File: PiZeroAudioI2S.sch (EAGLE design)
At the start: 52 parts, among them CN1 1X4-BIG, CON1 RPI-ZERO, J1 1X2-3.5MM, Q1 DMG2305UX, U1 TXB0104PWR, U2 LSM6DS33, U3 PCM5101A, U4 TPA3144D2PWPR, U5 DMMT5401

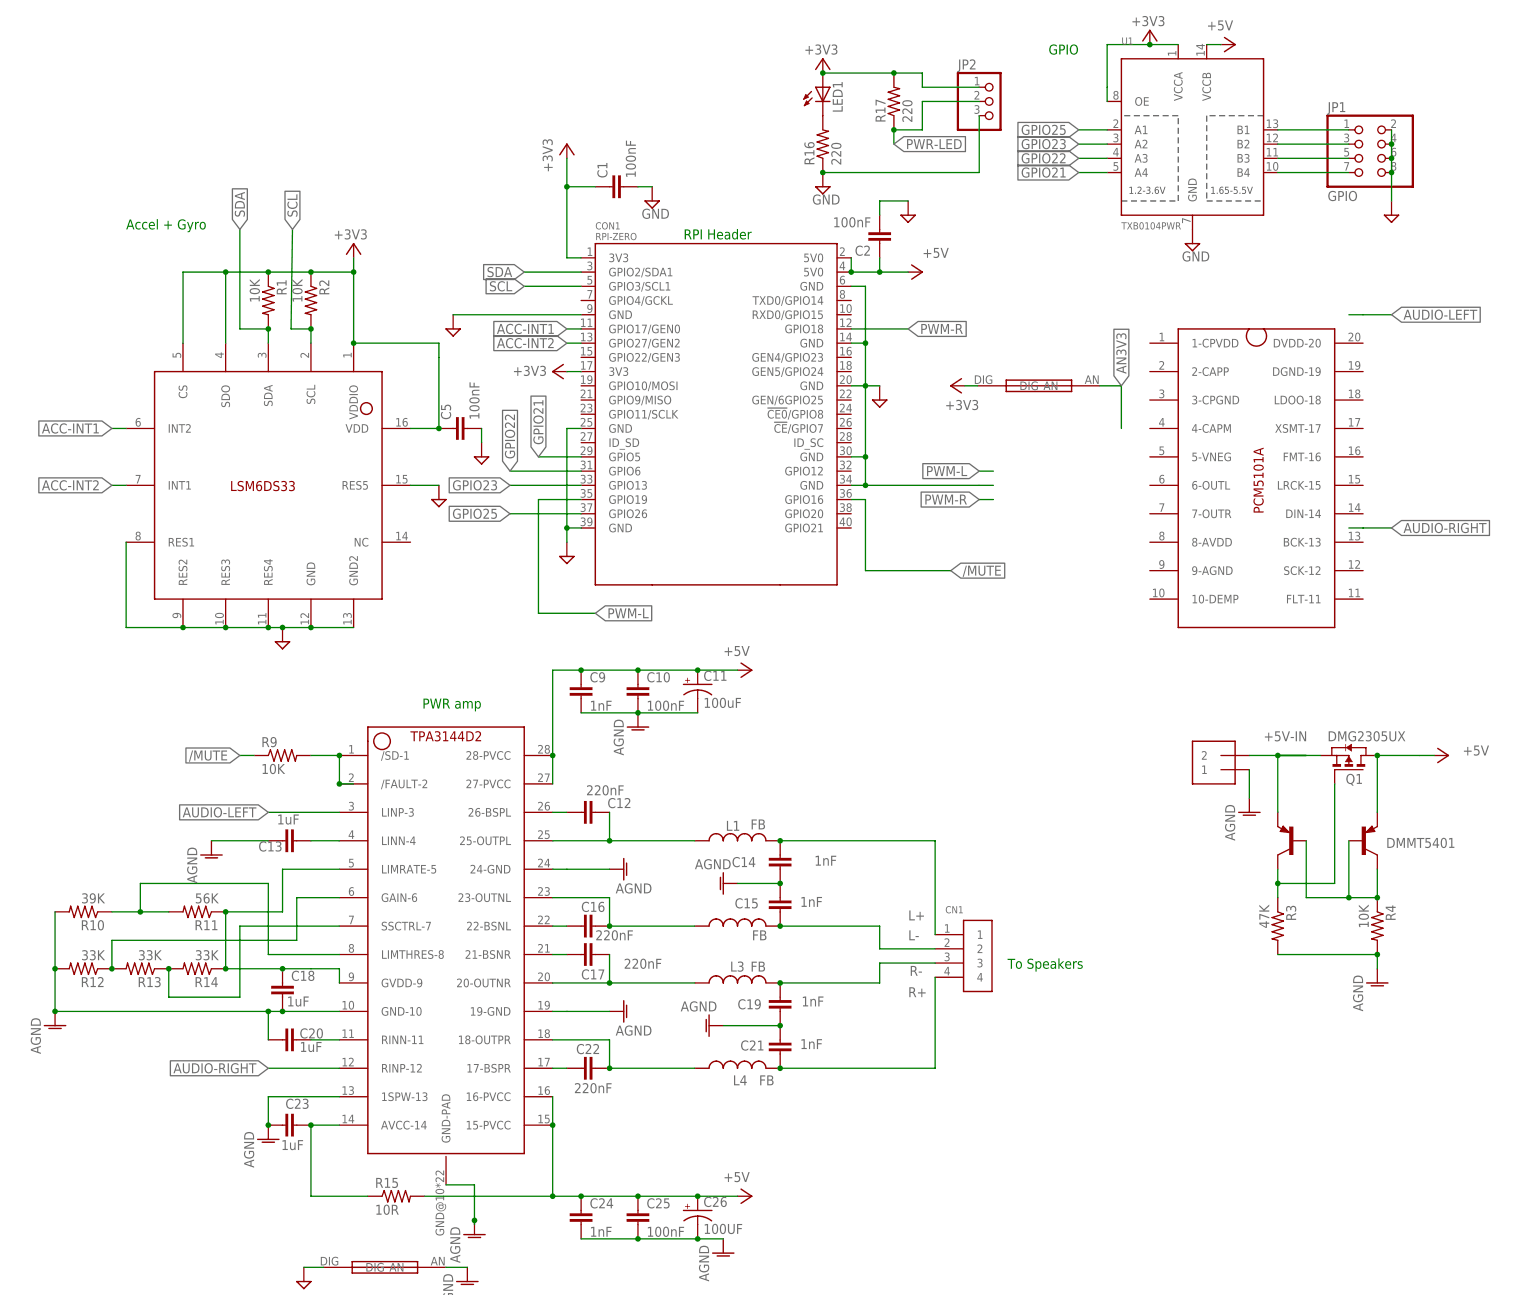
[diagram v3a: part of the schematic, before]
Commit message: Added I2Sboard
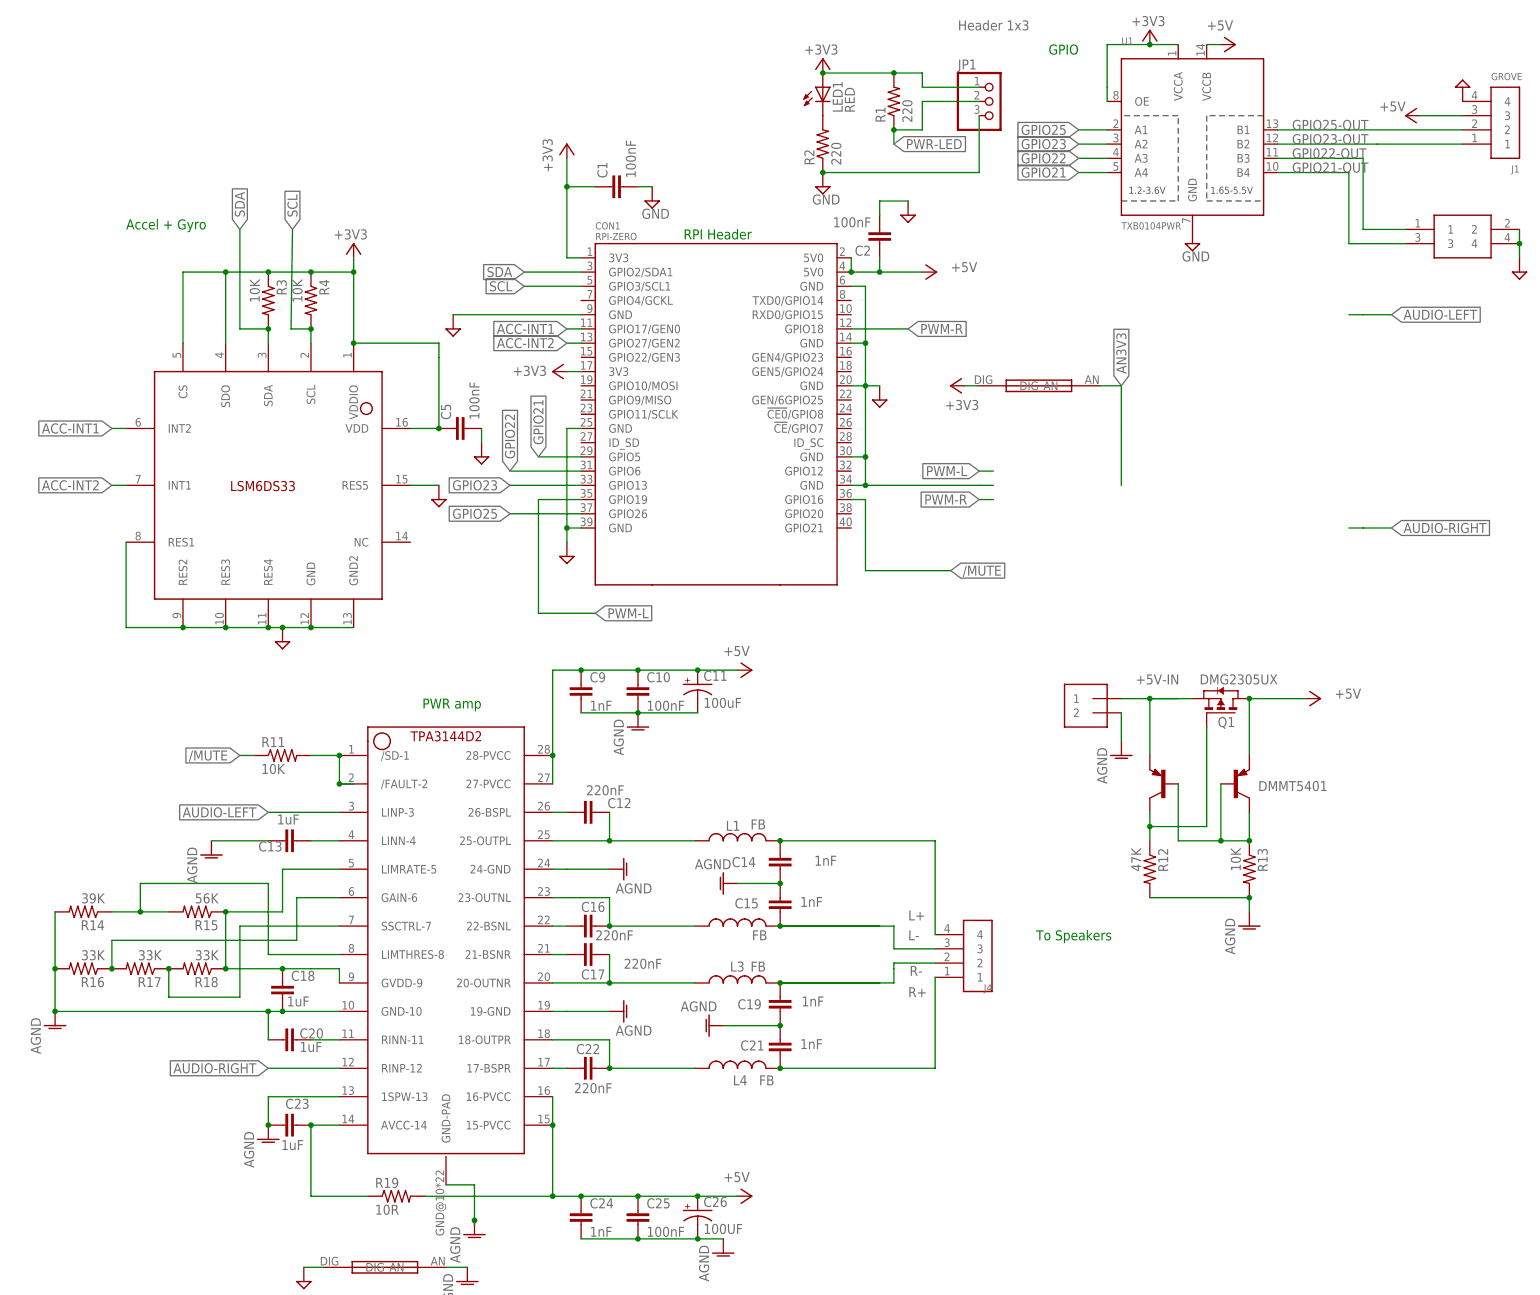
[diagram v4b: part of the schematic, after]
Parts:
- removed CN1: 1X4-BIG, adafruit:1X4-BIG
- removed JP2: (no value), adafruit:PINHD-1X3
- removed R10: 39K, adafruit:R-US_R0603
- removed R9: 10K, adafruit:R-US_R0603
- removed U3: PCM5101A, HappyBrackets:PCM5101A
- added J2: 2X2HEADER, HappyBrackets:2X2HEADER
- added J3: 2X1-LOCKING, HappyBrackets:2X1-LOCKING
- added J4: 4X1-LOCKING, HappyBrackets:4X1-LOCKING
- added R18: 33K, adafruit:R-US_R0603
- added R19: 10R, adafruit:R-US_R0603
- J1: value 1X2-3.5MM -> GROVE; device adafruit:1X2-3.5MM -> HappyBrackets:GROVE
- JP1: value GPIO -> Header 1x3; device adafruit:PINHD-2X4 -> adafruit:PINHD-1X3
- LED1: value (none) -> RED
- R1, R2: value 10K -> 220
- R11: value 56K -> 10K
- R12: value 33K -> 47K
- R13: value 33K -> 10K
- R14: value 33K -> 39K
- R15: value 10R -> 56K
- R16, R17: value 220 -> 33K
- R3: value 47K -> 10K
- U4: value TPA3144D2PWPR -> DMMT5401; device HappyBrackets:TPA3144D2PWPR -> HappyBrackets:DMMT5401
- U5: value DMMT5401 -> TPA3144D2PWPR; device HappyBrackets:DMMT5401 -> HappyBrackets:TPA3144D2PWPR
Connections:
- removed net N$1: Q1.G, R3.1, U5G$1.C
- removed net N$11: JP1.1, U1.B1
- removed net N$12: JP1.3, U1.B2
- removed net N$14: JP1.5, U1.B3
- removed net N$15: JP1.7, U1.B4
- removed net N$2: R4.1, U5G$1.B, U5G$2.B, U5G$2.C
- new net GPI022-OUT: J2.1, U1.B3
- new net GPIO21-OUT: J2.3, U1.B4
- new net GPIO23-OUT: J1.1, U1.B2
- new net GPIO25-OUT: J1.2, U1.B1
- new net N$22: R13.1, U4G$1.B, U4G$2.B, U4G$2.C
- new net N$27: Q1.G, R12.1, U4G$1.C
- net +3V3: now also JP1.1, R1.2, R3.1, R4.1; no longer JP2.1, R1.1, R17.2, R2.1
- net +5V: now also J1.3, R19.2, U4G$2.E, U5.15-PVCC, U5.16-PVCC, U5.27-PVCC, U5.28-PVCC; no longer R15.2, U4.15-PVCC, U4.16-PVCC, U4.27-PVCC, U4.28-PVCC, U5G$2.E
- net +5V-IN: now also J3.1, U4G$1.E; no longer J1.2, U5G$1.E
- net /MUTE: now also R11.1; no longer R9.1
- net AGND: now also J3.2, R13.2, R14.2, R16.2, U5.19-GND, U5.1SPW-13, U5.24-GND, U5.GND-10, U5.GND-PAD; no longer J1.1, R10.2, R3.2, R4.2, U4.19-GND, U4.1SPW-13, U4.24-GND, U4.GND-10, U4.GND-PAD
- net AUDIO-LEFT: now also U5.LINP-3; no longer U4.LINP-3
- net AUDIO-RIGHT: now also U5.RINP-12; no longer U4.RINP-12
- net GND: now also J1.4, J2.2, J2.4, JP1.3, R2.1; no longer JP1.2, JP1.4, JP1.6, JP1.8, JP2.3, R16.1
- net L+: now also J4.4; no longer CN1.1
- net L-: now also J4.3; no longer CN1.2
- net N$10: now also U5.17-BSPR; no longer U4.17-BSPR
- net N$13: now also U5.21-BSNR; no longer U4.21-BSNR
- net N$16: now also U5.22-BSNL; no longer U4.22-BSNL
- net N$17: now also U5.26-BSPL; no longer U4.26-BSPL
- net N$18: now also U5.25-OUTPL; no longer U4.25-OUTPL
- net N$19: now also U5.23-OUTNL; no longer U4.23-OUTNL
- net N$20: now also U5.20-OUTNR; no longer U4.20-OUTNR
- net N$21: now also U5.18-OUTPR; no longer U4.18-OUTPR
- net N$23: now also R16.1, R17.2, U5.GAIN-6; no longer R12.1, R13.2, U4.GAIN-6
- net N$24: now also R17.1, R18.2, U5.SSCTRL-7; no longer R13.1, R14.2, U4.SSCTRL-7
- net N$25: now also R14.1, R15.2, U5.LIMTHRES-8; no longer R10.1, R11.2, U4.LIMTHRES-8
- net N$26: now also R15.1, R18.1, U5.GVDD-9, U5.LIMRATE-5; no longer R11.1, R14.1, U4.GVDD-9, U4.LIMRATE-5
- net N$5: now also R11.2, U5./FAULT-2, U5./SD-1; no longer R9.2, U4./FAULT-2, U4./SD-1
- net N$6: now also R2.2; no longer R16.2
- net N$7: now also U5.LINN-4; no longer U4.LINN-4
- net N$8: now also U5.RINN-11; no longer U4.RINN-11
- net N$9: now also R19.1, U5.AVCC-14; no longer R15.1, U4.AVCC-14
- net PWR-LED: now also JP1.2, R1.1; no longer JP2.2, R17.1
- net R+: now also J4.1; no longer CN1.4
- net R-: now also J4.2; no longer CN1.3
- net SCL: now also R4.2; no longer R2.2
- net SDA: now also R3.2; no longer R1.2
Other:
- moved on the sheet: Q1, R1, R11, R12, R13, R14, R15, R16, R17, R2, R3, R4

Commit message: Performed layout
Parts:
- removed R16, R17, R18: 33K, adafruit:R-US_R0603
- removed R19: 10R, adafruit:R-US_R0603
- added C27, C30: 1uF, rcl:C-EUC0603
- added C28, C31: 1nF, rcl:C-EUC0603
- added C29: 220nF, rcl:C-EUC0603
- added C3: 0.1uF, rcl:C-EUC0603
- added C32, C6: 100nF, rcl:C-EUC0603
- added C33: 100UF, adafruit:CPOL-USCT3528
- added C4: 10uF, adafruit:CPOL-USCT3528
- added C7: 2.2nF, rcl:C-EUC0603
- added C8: 2.2uF, rcl:C-EUC0603
- added R10: 39K, adafruit:R-US_R0603
- added R5, R6: 470, adafruit:R-US_R0603
- added R7, R9: 10K, adafruit:R-US_R0603
- added R8: 47K, adafruit:R-US_R0603
- added U3: PCM5101A, HappyBrackets:PCM5101A
- C10: value 100nF -> 0.1uF
- C11: value 100uF -> 10uF
- C12: value 220nF -> 0.1uF
- C13: value 1uF -> 10uF; device rcl:C-EUC0603 -> adafruit:CPOL-USCT3528
- C14: value 1nF -> 0.1uF
- C15: value 1nF -> 10uF; device rcl:C-EUC0603 -> adafruit:CPOL-USCT3528
- C16, C22: value 220nF -> 1nF
- C17: value 220nF -> 100nF
- C18: value 1uF -> 100uF; device rcl:C-EUC0603 -> adafruit:CPOL-USCT3528
- C19, C24: value 1nF -> 220nF
- C23: value 1uF -> 220nF
- C25: value 100nF -> 1uF
- C26: value 100UF -> 1nF; device adafruit:CPOL-USCT3528 -> rcl:C-EUC0603
- C5: value 100nF -> 2.2nF
- C9: value 1nF -> 2.2uF
- R11: value 10K -> 56K
- R12: value 47K -> 33K
- R13: value 10K -> 33K
- R14: value 39K -> 33K
- R15: value 56K -> 10R
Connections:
- removed net PWM-L: CON1.GPIO19
- removed net PWM-R: CON1.GPIO18
- new net N$1: R5.1, U3.7-OUTR
- new net N$11: R6.1, U3.6-OUTL
- new net N$12: C10.1, C11.-, U3.LDOO-18
- new net N$2: C8.1, U3.5-VNEG
- new net N$3: C9.1, U3.4-CAPM
- new net N$4: C9.2, U3.2-CAPP
- new net PCM-CLK: CON1.GPIO18, U3.BCK-13
- new net PCM_DOUT: CON1.GPIO21, U3.DIN-14
- new net PCM_FS: CON1.GPIO19, U3.LRCK-15
- net +3V3: now also C14.2, C15.+, C6.1, U3.DVDD-20, U3.XSMT-17; no longer C5.1
- net +5V: now also C16.1, C17.1, C18.+, C31.1, C32.1, C33.+, R15.2; no longer C10.1, C11.+, C24.1, C25.1, C26.+, C9.1, R19.2
- net /MUTE: now also R7.1; no longer R11.1
- net AGND: now also C12.1, C13.-, C16.2, C17.2, C18.-, C21.2, C22.1, C26.2, C27.2, C28.1, C3.1, C30.2, C31.2, C32.2, C33.-, C4.-, C5.2, C7.2, C8.2, R10.2, R8.2, R9.2, U3.3-CPGND, U3.9-AGND; no longer C10.2, C11.-, C13.2, C14.2, C15.1, C18.2, C19.2, C21.1, C23.2, C24.2, C26.-, C9.2, R13.2, R14.2, R16.2
- net AN3V3: now also C12.2, C13.+, C3.2, C4.+, U3.1-CPVDD, U3.8-AVDD
- net AUDIO-LEFT: now also C7.1, R6.2
- net AUDIO-RIGHT: now also C5.1, R5.2
- net GND: now also C10.2, C11.+, C14.1, C15.-, C6.2, U3.10-DEMP, U3.DGND-19, U3.FLT-11, U3.FMT-16; no longer C5.2
- net L+: now also C21.1; no longer C14.1
- net L-: now also C22.2; no longer C15.2
- net N$10: now also C29.2; no longer C22.2
- net N$13: now also C24.2; no longer C17.2
- net N$16: now also C23.2; no longer C16.2
- net N$17: now also C19.2; no longer C12.2
- net N$18: now also C19.1; no longer C12.1
- net N$19: now also C23.1; no longer C16.1
- net N$20: now also C24.1; no longer C17.1
- net N$21: now also C29.1; no longer C22.1
- net N$22: now also R9.1; no longer R13.1
- net N$23: now also R12.1, R13.2; no longer R16.1, R17.2
- net N$24: now also R13.1, R14.2; no longer R17.1, R18.2
- net N$25: now also R10.1, R11.2; no longer R14.1, R15.2
- net N$26: now also C25.1, R11.1, R14.1; no longer C18.1, R15.1, R18.1
- net N$27: now also R8.1; no longer R12.1
- net N$5: now also R7.2; no longer R11.2
- net N$7: now also C20.1; no longer C13.1
- net N$8: now also C27.1; no longer C20.1
- net N$9: now also C30.1, R15.1; no longer C23.1, R19.1
- net R+: now also C28.2; no longer C21.2
- net R-: now also C26.1; no longer C19.1
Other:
- moved on the sheet: C10, C11, C12, C14, C16, C17, C19, C20, C21, C22, C23, C24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

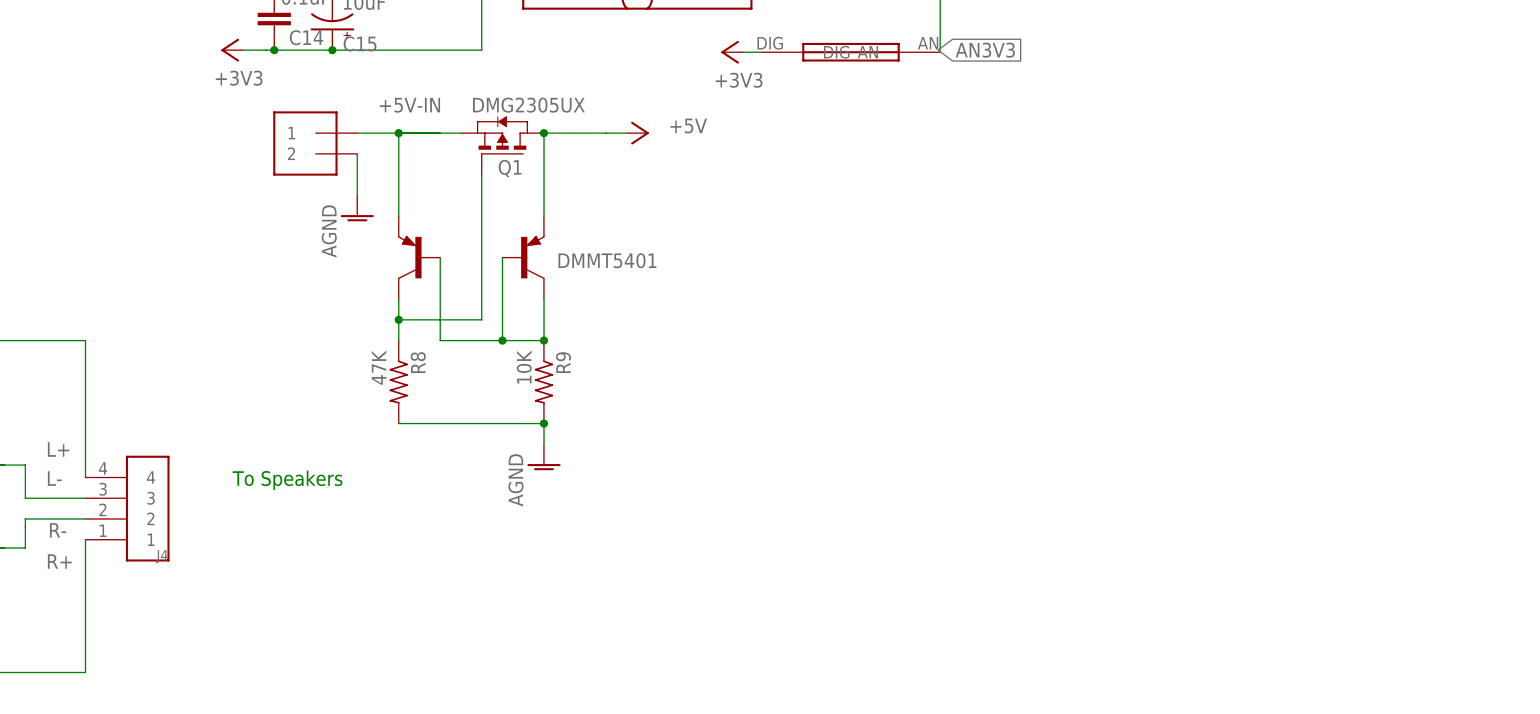
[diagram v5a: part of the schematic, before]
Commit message: Changed capacitor footprints
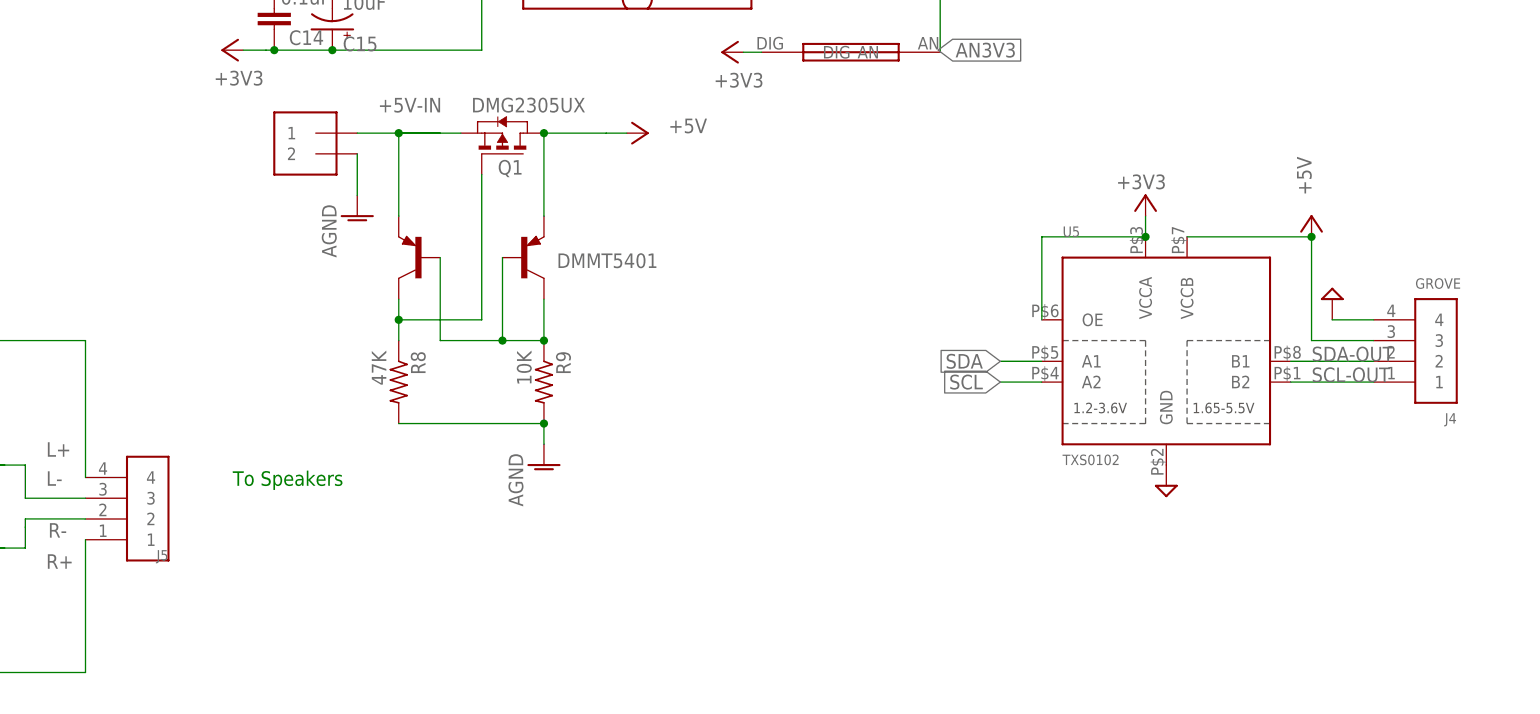
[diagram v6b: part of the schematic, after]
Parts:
- added J5: 4X1-LOCKING, HappyBrackets:4X1-LOCKING
- added U6: TPA3144D2PWPR, HappyBrackets:TPA3144D2PWPR
- C11, C13, C15, C18, C33, C4: device adafruit:CPOL-USCT3528 -> HappyBrackets:CAP-POLARISED
- J4: value 4X1-LOCKING -> GROVE; device HappyBrackets:4X1-LOCKING -> HappyBrackets:GROVE
- U5: value TPA3144D2PWPR -> TXS0102; device HappyBrackets:TPA3144D2PWPR -> adafruit:TXS0102
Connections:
- new net SCL-OUT: J4.1, U5.B2
- new net SDA-OUT: J4.2, U5.B1
- net +3V3: now also U5.OE, U5.VCCA
- net +5V: now also J4.3, U5.VCCB, U6.15-PVCC, U6.16-PVCC, U6.27-PVCC, U6.28-PVCC; no longer U5.15-PVCC, U5.16-PVCC, U5.27-PVCC, U5.28-PVCC
- net AGND: now also U6.19-GND, U6.1SPW-13, U6.24-GND, U6.GND-10, U6.GND-PAD; no longer U5.19-GND, U5.1SPW-13, U5.24-GND, U5.GND-10, U5.GND-PAD
- net AUDIO-LEFT: now also U6.LINP-3; no longer U5.LINP-3
- net AUDIO-RIGHT: now also U6.RINP-12; no longer U5.RINP-12
- net GND: now also J4.4, U5.GND
- net L+: now also J5.4; no longer J4.4
- net L-: now also J5.3; no longer J4.3
- net N$10: now also U6.17-BSPR; no longer U5.17-BSPR
- net N$13: now also U6.21-BSNR; no longer U5.21-BSNR
- net N$16: now also U6.22-BSNL; no longer U5.22-BSNL
- net N$17: now also U6.26-BSPL; no longer U5.26-BSPL
- net N$18: now also U6.25-OUTPL; no longer U5.25-OUTPL
- net N$19: now also U6.23-OUTNL; no longer U5.23-OUTNL
- net N$20: now also U6.20-OUTNR; no longer U5.20-OUTNR
- net N$21: now also U6.18-OUTPR; no longer U5.18-OUTPR
- net N$23: now also U6.GAIN-6; no longer U5.GAIN-6
- net N$24: now also U6.SSCTRL-7; no longer U5.SSCTRL-7
- net N$25: now also U6.LIMTHRES-8; no longer U5.LIMTHRES-8
- net N$26: now also U6.GVDD-9, U6.LIMRATE-5; no longer U5.GVDD-9, U5.LIMRATE-5
- net N$5: now also U6./FAULT-2, U6./SD-1; no longer U5./FAULT-2, U5./SD-1
- net N$7: now also U6.LINN-4; no longer U5.LINN-4
- net N$8: now also U6.RINN-11; no longer U5.RINN-11
- net N$9: now also U6.AVCC-14; no longer U5.AVCC-14
- net R+: now also J5.1; no longer J4.1
- net R-: now also J5.2; no longer J4.2
- net SCL: now also U5.A2
- net SDA: now also U5.A1
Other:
- moved on the sheet: J4
